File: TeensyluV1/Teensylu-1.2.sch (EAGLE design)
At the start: 101 parts, among them J1 M02POLAR, J11 M02POLAR, J12 M02POLAR, J2 MICROSD, J3 USB-MICRO-PTH, J4 M02POLAR, J5 4P-TERM-BLOCK284391-4, J6 39-29-3066, J7 HOTEND-1, J8 2x7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

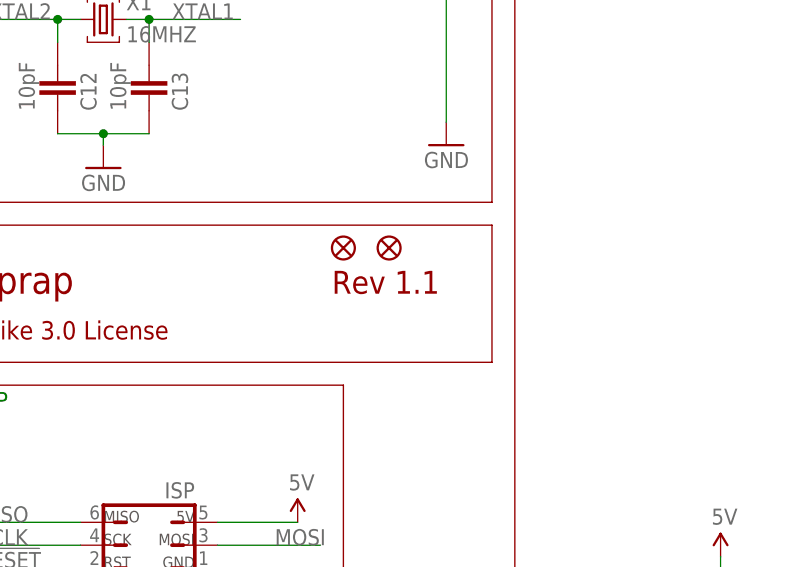
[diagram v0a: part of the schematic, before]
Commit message: Now with 4 layers!
The board is now 4 layers. This is to allow high current through the
planes. It also means less via's.
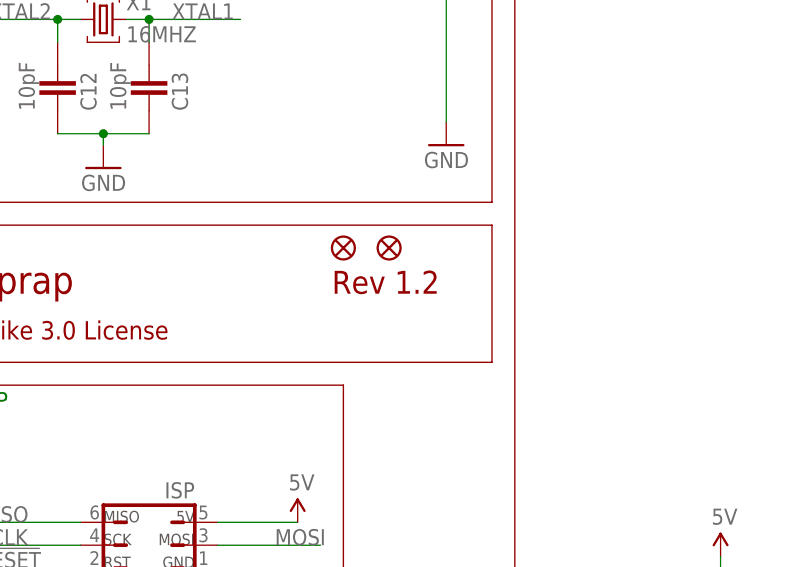
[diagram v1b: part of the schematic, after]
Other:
- note added: "Rev 1.2"
- note removed: "Rev 1.1"
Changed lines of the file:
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@@
 <text x="10.16" y="149.86" size="1.778" layer="91" font="vector">Power Acc</text>
 <text x="60.96" y="7.62" size="3.81" layer="94">TeensyluV1</text>
-<text x="175.26" y="7.62" size="2.54" layer="94">Rev 1.1</text>
+<text x="175.26" y="7.62" size="2.54" layer="94">Rev 1.2</text>
 <text x="111.76" y="7.62" size="3.048" layer="94">Control for Reprap</text>
 <text x="63.5" y="2.54" size="2.032" layer="94">Licensed under the Creative Commons Attributions ShareAlike 3.0 License</text>
